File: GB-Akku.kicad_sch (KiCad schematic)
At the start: 10 parts, among them J1 Conn_01x01_Socket, J2 Conn_01x01_Socket, J3 Conn_01x01_Socket, J4 Conn_01x01_Socket

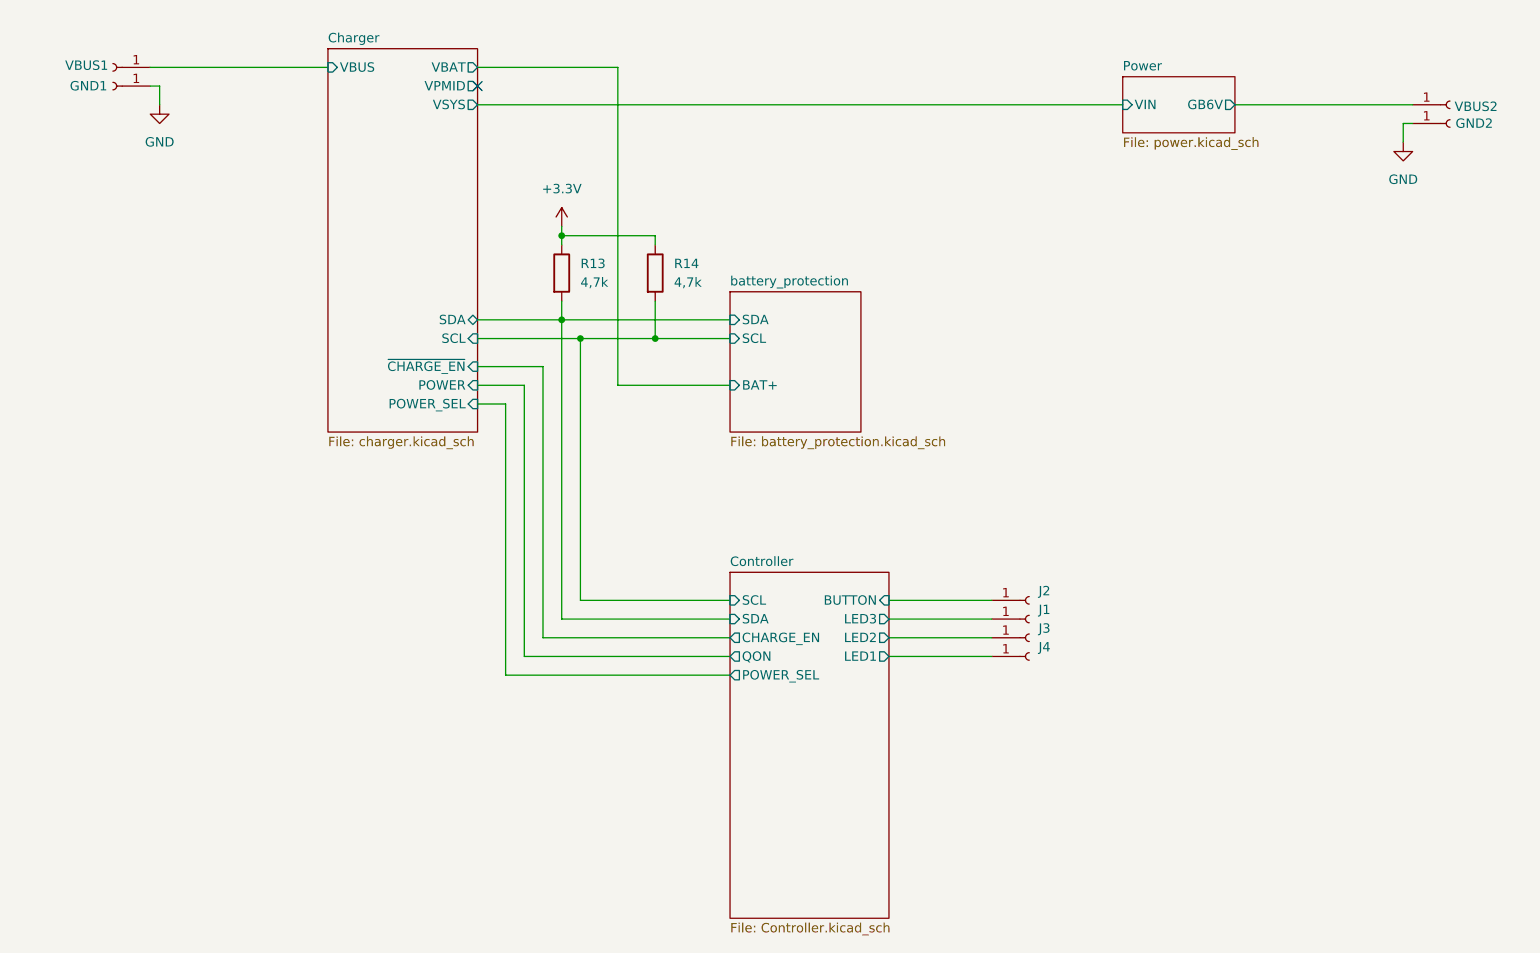
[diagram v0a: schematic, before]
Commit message: STM32 BOOT0 Pin fixed
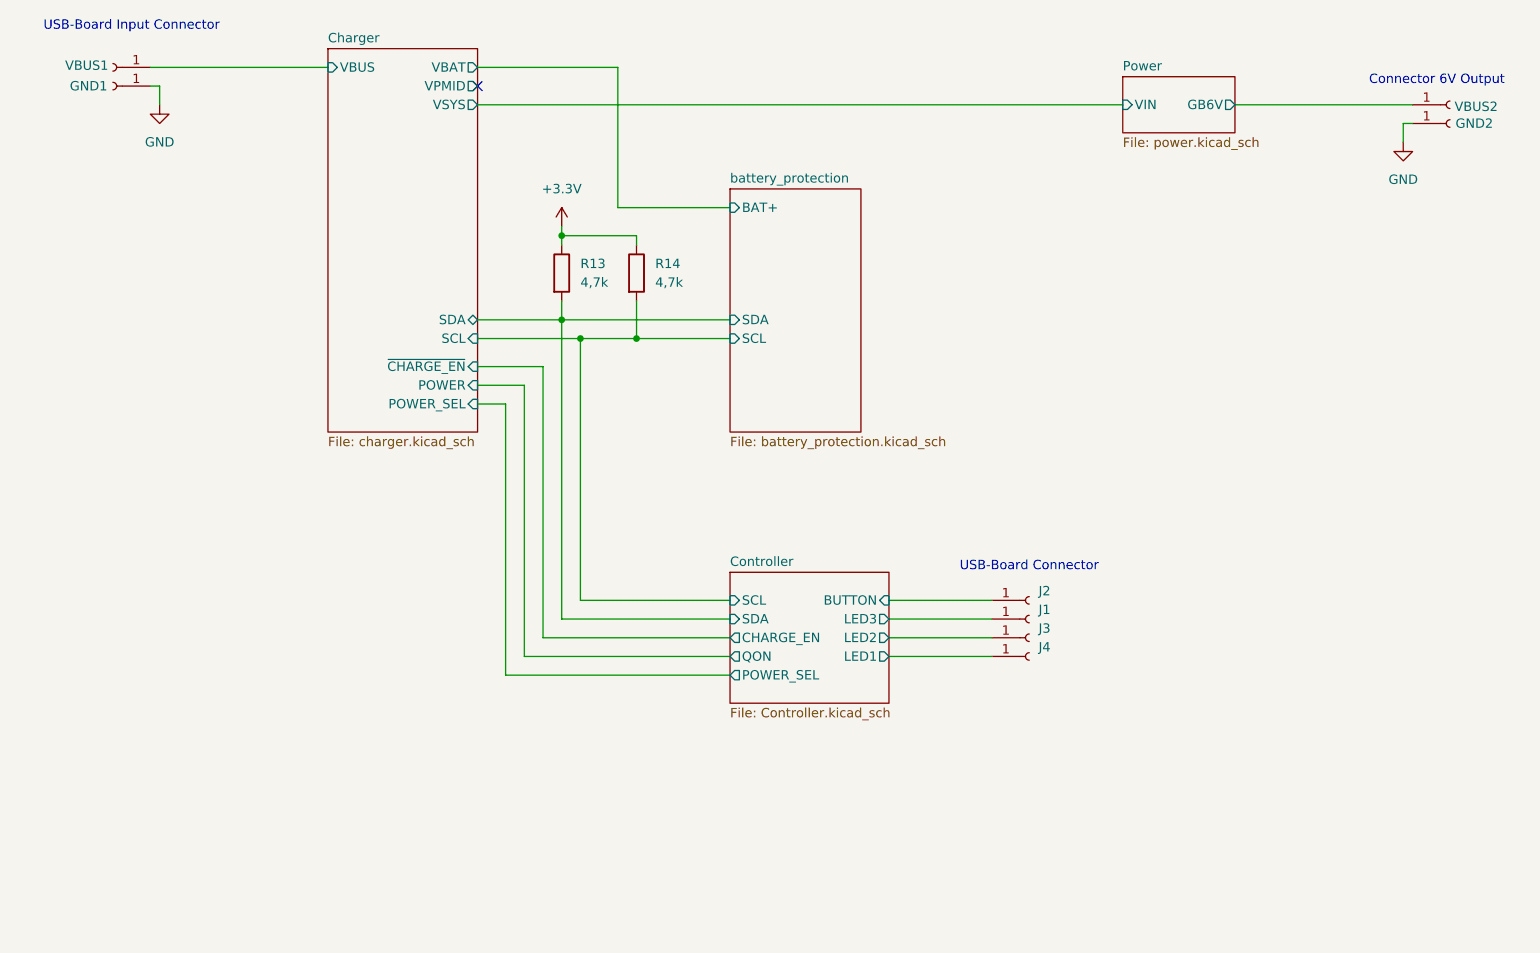
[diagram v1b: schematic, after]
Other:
- note added: "Connector 6V Output"
- note added: "USB-Board Connector"
- note added: "USB-Board Input Connector"
- moved on the sheet: R14
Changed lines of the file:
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@@
 	(paper "A4")
-	(junction
-		(at 116.84 68.58)
-		(diameter 0)
-		(color 0 0 0 0)
-	)
 	(junction
 		(at 104.14 66.04)
@@
 	)
 	(junction
+		(at 114.3 68.58)
+		(diameter 0)
+		(color 0 0 0 0)
+	)
+	(junction
 		(at 106.68 68.58)
 		(diameter 0)
@@
 	(wire
 		(pts
-			(xy 111.76 74.93) (xy 127 74.93)
+			(xy 111.76 50.8) (xy 127 50.8)
 		)
 		(stroke
@@
 	(wire
 		(pts
-			(xy 111.76 31.75) (xy 111.76 74.93)
+			(xy 111.76 31.75) (xy 111.76 50.8)
 		)
 		(stroke
@@
 	(wire
 		(pts
-			(xy 104.14 54.61) (xy 116.84 54.61)
+			(xy 104.14 54.61) (xy 114.3 54.61)
 		)
 		(stroke
@@
 	(wire
 		(pts
+			(xy 114.3 68.58) (xy 127 68.58)
+		)
+		(stroke
+			(width 0)
+			(type default)
+		)
+	)
+	(wire
+		(pts
 			(xy 101.6 72.39) (xy 92.71 72.39)
 		)
@@
 	(wire
 		(pts
-			(xy 106.68 68.58) (xy 116.84 68.58)
+			(xy 106.68 68.58) (xy 114.3 68.58)
 		)
 		(stroke
@@
 	(wire
 		(pts
-			(xy 116.84 54.61) (xy 116.84 55.88)
+			(xy 114.3 54.61) (xy 114.3 55.88)
 		)
 		(stroke
@@
 	(wire
 		(pts
-			(xy 116.84 68.58) (xy 127 68.58)
-		)
-		(stroke
-			(width 0)
-			(type default)
-		)
-	)
-	(wire
-		(pts
 			(xy 104.14 66.04) (xy 127 66.04)
 		)
@@
 	(wire
 		(pts
-			(xy 116.84 63.5) (xy 116.84 68.58)
+			(xy 114.3 63.5) (xy 114.3 68.58)
 		)
 		(stroke
@@
 			(width 0)
 			(type default)
+		)
+	)
+	(text "Connector 6V Output"
+		(exclude_from_sim no)
+		(at 223.012 33.528 0)
+		(effects
+			(font
+				(size 1.27 1.27)
+			)
+		)
+	)
+	(text "USB-Board Input Connector"
+		(exclude_from_sim no)
+		(at 45.72 26.162 0)
+		(effects
+			(font
+				(size 1.27 1.27)
+			)
+		)
+	)
+	(text "USB-Board Connector"
+		(exclude_from_sim no)
+		(at 167.64 99.568 0)
+		(effects
+			(font
+				(size 1.27 1.27)
+			)
 		)
 	)
@@
 	(symbol
 		(lib_id "Device:R")
-		(at 116.84 59.69 0)
+		(at 114.3 59.69 0)
 		(unit 1)
 		(exclude_from_sim no)
@@
 		(fields_autoplaced yes)
 		(property "Reference" "R14"
-			(at 119.38 58.4199 0)
+			(at 116.84 58.4199 0)
 			(effects
 				(font
@@
 		)
 		(property "Value" "4,7k"
-			(at 119.38 60.9599 0)
+			(at 116.84 60.9599 0)
 			(effects
 				(font
@@
 		)
 		(property "Footprint" "Resistor_SMD:R_0603_1608Metric"
-			(at 115.062 59.69 90)
+			(at 112.522 59.69 90)
 			(effects
 				(font
@@
 		)
 		(property "Datasheet" "~"
-			(at 116.84 59.69 0)
+			(at 114.3 59.69 0)
 			(effects
 				(font
@@
 		)
 		(property "Description" "Resistor"
-			(at 116.84 59.69 0)
+			(at 114.3 59.69 0)
 			(effects
 				(font
@@
 	)
 	(sheet
-		(at 127 62.23)
-		(size 17.78 19.05)
+		(at 127 48.26)
+		(size 17.78 33.02)
 		(fields_autoplaced yes)
 		(stroke
@@
 		)
 		(property "Sheetname" "battery_protection"
-			(at 127 61.5184 0)
+			(at 127 47.5484 0)
 			(effects
 				(font
@@
 		)
 		(pin "BAT+" input
-			(at 127 74.93 180)
+			(at 127 50.8 180)
 			(effects
 				(font
@@
 	(sheet
 		(at 127 100.33)
-		(size 21.59 46.99)
+		(size 21.59 17.78)
 		(fields_autoplaced yes)
 		(stroke
@@
 		)
 		(property "Sheetfile" "Controller.kicad_sch"
-			(at 127 147.9046 0)
-			(effects
-				(font
+			(at 127 118.6946 0)
+			(effects
+				(font
